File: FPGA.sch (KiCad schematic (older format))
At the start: 22 parts, among them J1 Conn_Coaxial, J101 Conn_02x20_Odd_Even, J102 Conn_02x07_Odd_Even, J103 Conn_02x07_Odd_Even, J2 Conn_Coaxial, J3 Conn_Coaxial, J4 Conn_Coaxial, J5 Conn_Coaxial, J6 Conn_Coaxial, SW101 SW_Push, U101 ASDMB-xxxMHz

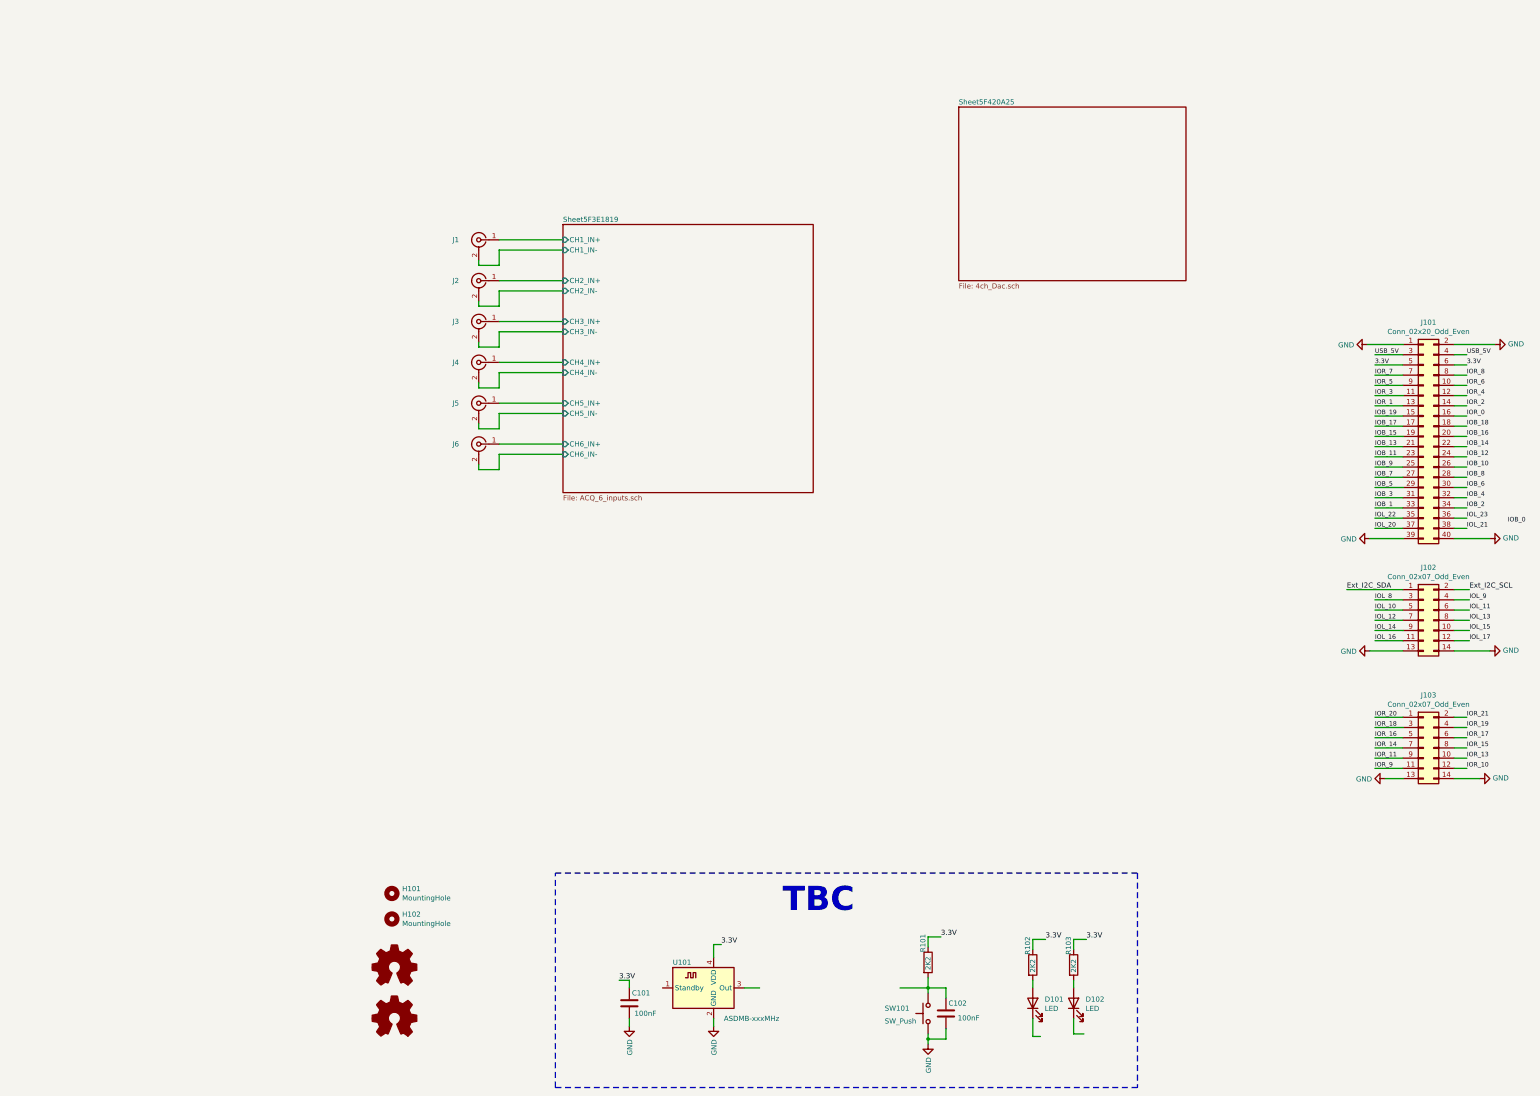
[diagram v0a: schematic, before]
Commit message: initial placement of all ADC/DAC blocks and added FPGA
Signed-off-by: Alexis Jeandet <alexis.jeandet@member.fsf.org>
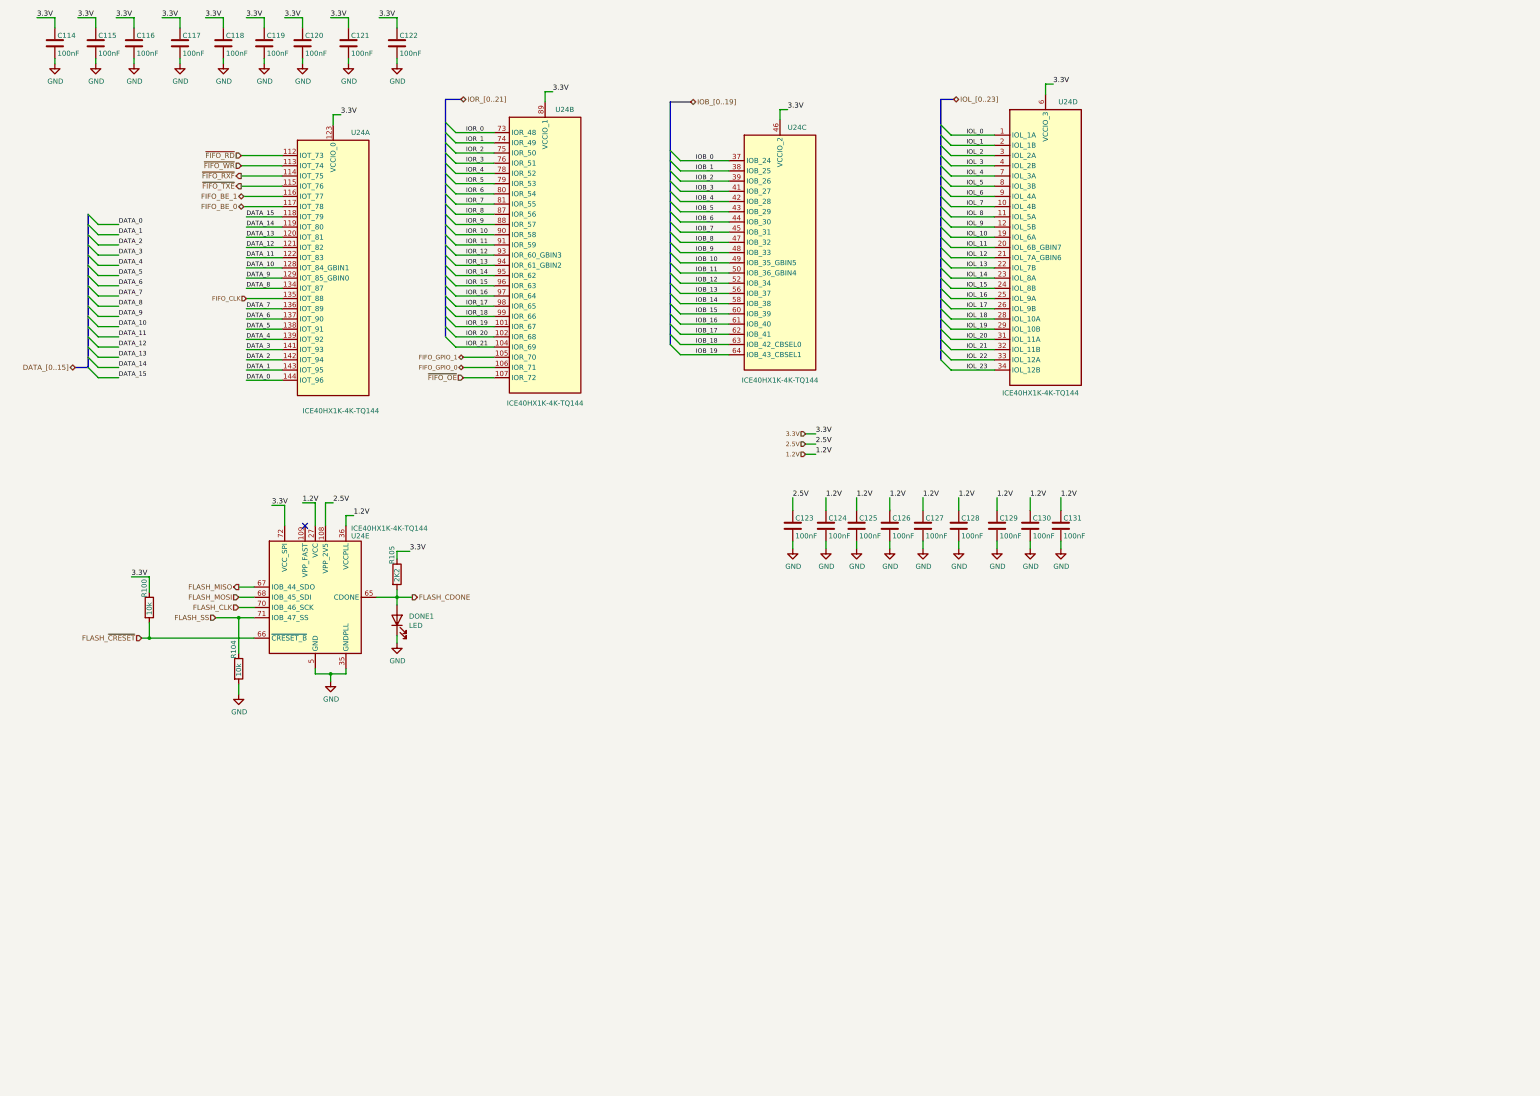
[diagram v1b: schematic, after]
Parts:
- removed C101, C102: 100nF, Capacitor_SMD:C_0402_1005Metric, symbol Device:C
- removed D101, D102: LED, Resistor_SMD:R_0603_1608Metric_Pad1.05x0.95mm_HandSolder, symbol Device:LED
- removed H101, H102: MountingHole, MountingHole:MountingHole_2.7mm_M2.5, symbol Mechanical:MountingHole
- removed J1, J2, J3, J4, J5, J6: Conn_Coaxial, Connector_Coaxial:SMB_Jack_Vertical, symbol Connector:Conn_Coaxial
- removed J101: Conn_02x20_Odd_Even, Connector_PinHeader_2.54mm:PinHeader_2x20_P2.54mm_Vertical, symbol Connector_Generic:Conn_02x20_Odd_Even
- removed J102, J103: Conn_02x07_Odd_Even, Connector_PinHeader_2.54mm:PinHeader_2x07_P2.54mm_Vertical, symbol Connector_Generic:Conn_02x07_Odd_Even
- removed LOGO101: Logo_Open_Hardware_Small, Symbol:OSHW-Logo2_9.8x8mm_SilkScreen, symbol Graphic:Logo_Open_Hardware_Small
- removed LOGO102: Logo_Open_Hardware_Small, Symbol:KiCad-Logo2_6mm_SilkScreen, symbol Graphic:Logo_Open_Hardware_Small
- removed R101, R102, R103: 2K2, Resistor_SMD:R_0402_1005Metric, symbol Device:R
- removed SW101: SW_Push, Button_Switch_SMD:SW_SPST_EVQPE1, symbol Switch:SW_Push
- removed U101: ASDMB-xxxMHz, Oscillator:Oscillator_SMD_Abracon_ASDMB-4Pin_2.5x2.0mm, symbol Oscillator:ASDMB-xxxMHz
- added C301, C302, C303, C305, C306, C307, C308, C309, C310, C311, C312, C313, C314, C315, C316, C317, C318, C319: 100nF, Capacitor_SMD:C_0402_1005Metric, symbol Device:C
- added DONE401: LED, Resistor_SMD:R_0603_1608Metric_Pad1.05x0.95mm_HandSolder, symbol Device:LED
- added R305, R401: 10k, Resistor_SMD:R_0402_1005Metric, symbol Device:R
- added R306: 2K2, Resistor_SMD:R_0402_1005Metric, symbol Device:R
- added U24: ICE40HX1K-4K-TQ144, Package_QFP:TQFP-144_20x20mm_P0.5mm, symbol ICE40:ICE40HX1K-4K-TQ144
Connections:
- net GND: now also C301.2, C302.2, C303.2, C305.2, C306.2, C307.2, C308.2, C309.2, C310.2, C311.2, C312.2, C313.2, C314.2, C315.2, C316.2, C317.2, C318.2, C319.2, DONE401.1 (K), R401.2, U24.103 (GND), U24.127 (GNDPLL), U24.13 (GND), U24.132 (GND), U24.14 (GND), U24.140 (GND), U24.35 (GNDPLL), U24.5 (GND), U24.53 (GNDPLL), U24.59 (GND), U24.69 (GND), U24.86 (GND)
- net IOB_0: now also U24.37 (IOB_24)
- net IOB_1: now also U24.38 (IOB_25)
- net IOB_10: now also U24.49 (IOB_35_GBIN5)
- net IOB_11: now also U24.50 (IOB_36_GBIN4)
- net IOB_12: now also U24.52 (IOB_34)
- net IOB_13: now also U24.56 (IOB_37)
- net IOB_14: now also U24.58 (IOB_38)
- net IOB_15: now also U24.60 (IOB_39)
- net IOB_16: now also U24.61 (IOB_40)
- net IOB_17: now also U24.62 (IOB_41)
- net IOB_18: now also U24.63 (IOB_42_CBSEL0)
- net IOB_19: now also U24.64 (IOB_43_CBSEL1)
- net IOB_2: now also U24.39 (IOB_26)
- net IOB_3: now also U24.41 (IOB_27)
- net IOB_4: now also U24.42 (IOB_28)
- net IOB_5: now also U24.43 (IOB_29)
- net IOB_6: now also U24.44 (IOB_30)
- net IOB_7: now also U24.45 (IOB_31)
- net IOB_8: now also U24.47 (IOB_32)
- net IOB_9: now also U24.48 (IOB_33)
- net IOL_10: now also U24.19 (IOL_6A)
- net IOL_11: now also U24.20 (IOL_6B_GBIN7)
- net IOL_12: now also U24.21 (IOL_7A_GBIN6)
- net IOL_13: now also U24.22 (IOL_7B)
- net IOL_14: now also U24.23 (IOL_8A)
- net IOL_15: now also U24.24 (IOL_8B)
- net IOL_16: now also U24.25 (IOL_9A)
- net IOL_17: now also U24.26 (IOL_9B)
- net IOL_20: now also U24.31 (IOL_11A)
- net IOL_21: now also U24.32 (IOL_11B)
- net IOL_22: now also U24.33 (IOL_12A)
- net IOL_23: now also U24.34 (IOL_12B)
- net IOL_8: now also U24.11 (IOL_5A)
- net IOL_9: now also U24.12 (IOL_5B)
- net IOR_0: now also U24.73 (IOR_48)
- net IOR_1: now also U24.74 (IOR_49)
- net IOR_10: now also U24.90 (IOR_58)
- net IOR_11: now also U24.91 (IOR_59)
- net IOR_13: now also U24.94 (IOR_61_GBIN2)
- net IOR_14: now also U24.95 (IOR_62)
- net IOR_15: now also U24.96 (IOR_63)
- net IOR_16: now also U24.97 (IOR_64)
- net IOR_17: now also U24.98 (IOR_65)
- net IOR_18: now also U24.99 (IOR_66)
- net IOR_19: now also U24.101 (IOR_67)
- net IOR_2: now also U24.75 (IOR_50)
- net IOR_20: now also U24.102 (IOR_68)
- net IOR_21: now also U24.104 (IOR_69)
- net IOR_3: now also U24.76 (IOR_51)
- net IOR_4: now also U24.78 (IOR_52)
- net IOR_5: now also U24.79 (IOR_53)
- net IOR_6: now also U24.80 (IOR_54)
- net IOR_7: now also U24.81 (IOR_55)
- net IOR_8: now also U24.87 (IOR_56)
- net IOR_9: now also U24.88 (IOR_57)
- new net 2.5V: C305.1, U24.108 (VPP_2V5)
- new net DATA_0: U24.144 (IOT_96)
- new net DATA_1: U24.143 (IOT_95)
- new net DATA_10: U24.128 (IOT_84_GBIN1)
- new net DATA_11: U24.122 (IOT_83)
- new net DATA_12: U24.121 (IOT_82)
- new net DATA_13: U24.120 (IOT_81)
- new net DATA_14: U24.119 (IOT_80)
- new net DATA_15: U24.118 (IOT_79)
- new net DATA_2: U24.142 (IOT_94)
- new net DATA_3: U24.141 (IOT_93)
- new net DATA_4: U24.139 (IOT_92)
- new net DATA_5: U24.138 (IOT_91)
- new net DATA_6: U24.137 (IOT_90)
- new net DATA_7: U24.136 (IOT_89)
- new net DATA_8: U24.134 (IOT_87)
- new net DATA_9: U24.129 (IOT_85_GBIN0)
- new net FIFO_BE_0: U24.117 (IOT_78)
- new net FIFO_BE_1: U24.116 (IOT_77)
- new net FIFO_CLK: U24.135 (IOT_88)
- new net FIFO_GPIO_0: U24.106 (IOR_71)
- new net FIFO_GPIO_1: U24.105 (IOR_70)
- new net FLASH_CDONE: DONE401.2 (A), R306.2, U24.65 (CDONE)
- new net FLASH_CLK: U24.70 (IOB_46_SCK)
- new net FLASH_MISO: U24.67 (IOB_44_SDO)
- new net FLASH_MOSI: U24.68 (IOB_45_SDI)
- new net FLASH_SS: R401.1, U24.71 (IOB_47_SS)
- new net FLASH_~CRESET: R305.2, U24.66 (~CRESET_B)
- new net IOL_0: U24.1 (IOL_1A)
- new net IOL_1: U24.2 (IOL_1B)
- new net IOL_18: U24.28 (IOL_10A)
- new net IOL_19: U24.29 (IOL_10B)
- new net IOL_2: U24.3 (IOL_2A)
- new net IOL_3: U24.4 (IOL_2B)
- new net IOL_4: U24.7 (IOL_3A)
- new net IOL_5: U24.8 (IOL_3B)
- new net IOL_6: U24.9 (IOL_4A)
- new net IOL_7: U24.10 (IOL_4B)
- new net IOR_12: U24.93 (IOR_60_GBIN3)
- new net VCC: C306.1, C307.1, C313.1, C314.1, C315.1, C317.1, C318.1, C319.1, U24.111 (VCC), U24.126 (VCCPLL), U24.27 (VCC), U24.36 (VCCPLL), U24.40 (VCC), U24.51 (VCC), U24.54 (VCCPLL), U24.92 (VCC)
- new net VCCIO_0: C301.1, C302.1, C303.1, C308.1, C309.1, C310.1, C311.1, C312.1, C316.1, R305.1, R306.1, U24.100 (VCCIO_1), U24.123 (VCCIO_0), U24.131 (VCCIO_0), U24.133 (VCCIO_0), U24.30 (VCCIO_3), U24.46 (VCCIO_2), U24.57 (VCCIO_2), U24.6 (VCCIO_3), U24.72 (VCC_SPI), U24.89 (VCCIO_1)
- new net ~FIFO_OE: U24.107 (IOR_72)
- new net ~FIFO_RD: U24.112 (IOT_73)
- new net ~FIFO_RXF: U24.114 (IOT_75)
- new net ~FIFO_TXE: U24.115 (IOT_76)
- new net ~FIFO_WR: U24.113 (IOT_74)
- no-connect marks 0 -> 1
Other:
- note removed: "TBC"
